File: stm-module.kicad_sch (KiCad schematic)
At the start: 15 parts, among them SW1 Reset, U1 STM32G474RETx, U2 TPS7A20xxxDBV, Y1 Crystal_GND24

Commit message: add crystal
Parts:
- removed Y1: Crystal_GND24, Crystal:Crystal_SMD_5032-4Pin_5.0x3.2mm, symbol Device:Crystal_GND24
- added C10, C11: 15pF, Capacitor_THT:C_Disc_D5.0mm_W2.5mm_P5.00mm, symbol Device:C
- added Y1: Crystal, Crystal:Crystal_SMD_0603-2Pin_6.0x3.5mm, symbol Device:Crystal
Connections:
- net GND: now also C10.1, C11.1
- net at U1.5 (PF0): now also C10.2, Y1.2
- net at U1.6 (PF1): now also C11.2, Y1.1

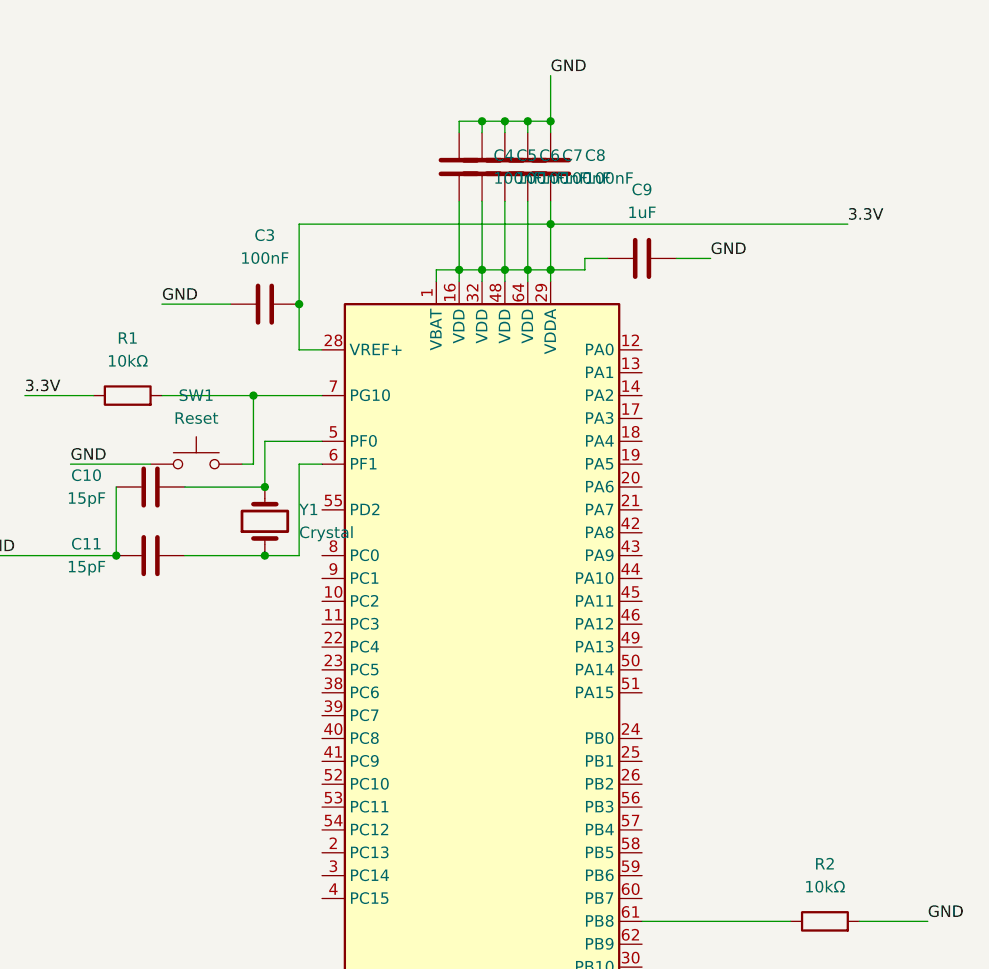
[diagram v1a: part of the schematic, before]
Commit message: add more caps
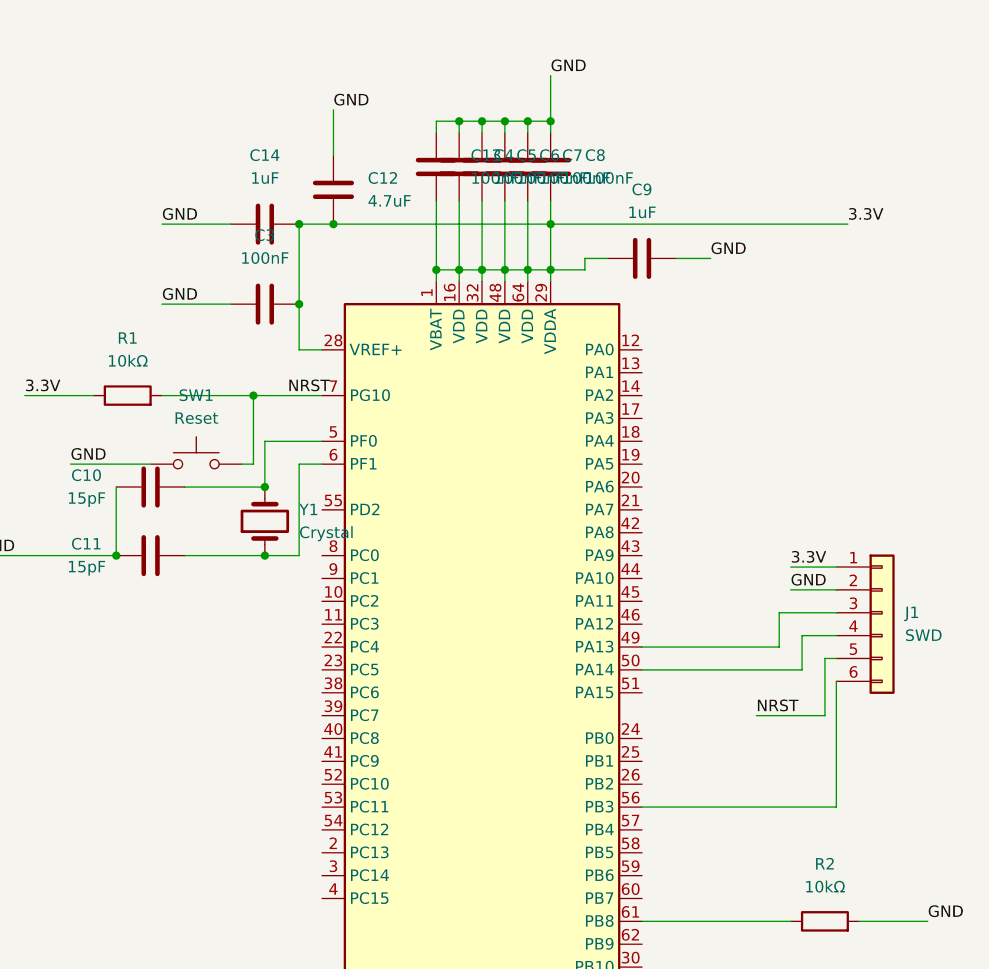
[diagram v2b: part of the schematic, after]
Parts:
- added C12: 4.7uF, Capacitor_SMD:C_0805_2012Metric, symbol Device:C
- added C13: 100nF, Capacitor_SMD:C_0805_2012Metric, symbol Device:C
- added C14: 1uF, Capacitor_SMD:C_0805_2012Metric, symbol Device:C
- added J1: SWD, Connector_PinHeader_2.54mm:PinHeader_1x06_P2.54mm_Vertical, symbol Connector_Generic:Conn_01x06
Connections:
- net 3.3V: now also C12.1, C13.1, C14.2, J1.1 (Pin_1)
- net GND: now also C12.2, C13.2, C14.1, J1.2 (Pin_2)
- net at U1.49 (PA13): now also J1.3 (Pin_3)
- net at U1.50 (PA14): now also J1.4 (Pin_4)
- net at U1.56 (PB3): now also J1.6 (Pin_6)
- net NRST: now reaches R1.2, SW1.2, U1.7 (PG10)
- net NRST: now also J1.5 (Pin_5)

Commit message: pcb work
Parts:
- added J2: connectorL, Connector_PinHeader_2.54mm:PinHeader_2x20_P2.54mm_Vertical, symbol Connector_Generic:Conn_02x20_Odd_Even
- added J3: connectorR, Connector_PinHeader_2.54mm:PinHeader_2x20_P2.54mm_Vertical, symbol Connector_Generic:Conn_02x20_Odd_Even
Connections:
- net GND: now also J2.1 (Pin_1)
- net PC2: now reaches U1.10 (PC2)
- net PC3: now reaches U1.11 (PC3)
- net PA0: now reaches U1.12 (PA0)
- net PA1: now reaches U1.13 (PA1)
- net PA2: now reaches U1.14 (PA2)
- net PA3: now reaches U1.17 (PA3)
- net PA4: now reaches U1.18 (PA4)
- net PA5: now reaches U1.19 (PA5)
- net PC13: now reaches U1.2 (PC13)
- net PA6: now reaches U1.20 (PA6)
- net PA7: now reaches U1.21 (PA7)
- net PC4: now reaches U1.22 (PC4)
- net PC5: now reaches U1.23 (PC5)
- net PB0: now reaches U1.24 (PB0)
- net PB1: now reaches U1.25 (PB1)
- net PB2: now reaches U1.26 (PB2)
- net PC14: now reaches U1.3 (PC14)
- net PB10: now reaches U1.30 (PB10)
- net PB11: now reaches U1.33 (PB11)
- net PB12: now reaches U1.34 (PB12)
- net PB13: now reaches U1.35 (PB13)
- net PB14: now reaches U1.36 (PB14)
- net PB15: now reaches U1.37 (PB15)
- net PC6: now reaches U1.38 (PC6)
- net PC7: now reaches U1.39 (PC7)
- net PC15: now reaches U1.4 (PC15)
- net PC8: now reaches U1.40 (PC8)
- net PC9: now reaches U1.41 (PC9)
- net PA8: now reaches U1.42 (PA8)
- net PA9: now reaches U1.43 (PA9)
- net PA10: now reaches U1.44 (PA10)
- net PA11: now reaches U1.45 (PA11)
- net PA12: now reaches U1.46 (PA12)
- net PA13: now reaches J1.3 (Pin_3), U1.49 (PA13)
- net PA14: now reaches J1.4 (Pin_4), U1.50 (PA14)
- net PA15: now reaches U1.51 (PA15)
- net PC10: now reaches U1.52 (PC10)
- net PC11: now reaches U1.53 (PC11)
- net PC12: now reaches U1.54 (PC12)
- net PD2: now reaches U1.55 (PD2)
- net PB3: now reaches J1.6 (Pin_6), U1.56 (PB3)
- net PB4: now reaches U1.57 (PB4)
- net PB5: now reaches U1.58 (PB5)
- net PB6: now reaches U1.59 (PB6)
- net PB7: now reaches U1.60 (PB7)
- net PB8: now reaches R2.1, U1.61 (PB8)
- net PB9: now reaches U1.62 (PB9)
- net PC0: now reaches U1.8 (PC0)
- net PC1: now reaches U1.9 (PC1)
- net 3.3V renamed +3.3V
- net 5V renamed +5V
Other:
- moved on the sheet: C1, C2, C9, J1, SW1, U2, Y1

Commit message: updates
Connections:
- net +3.3V: now also J3.15 (Pin_15), J3.30 (Pin_30)
- net GND: now also J3.1 (Pin_1), J3.17 (Pin_17), J3.18 (Pin_18), J3.19 (Pin_19), J3.20 (Pin_20), J3.21 (Pin_21), J3.22 (Pin_22), J3.23 (Pin_23), J3.24 (Pin_24), J3.25 (Pin_25), J3.26 (Pin_26), J3.27 (Pin_27), J3.28 (Pin_28)
- net PA10: now also J3.3 (Pin_3)
- net PA11: now also J3.4 (Pin_4)
- net PA12: now also J3.2 (Pin_2)
- net PA3: now also J3.40 (Pin_40)
- net PA4: now also J3.39 (Pin_39)
- net PA5: now also J3.38 (Pin_38)
- net PA6: now also J3.37 (Pin_37)
- net PA7: now also J3.36 (Pin_36)
- net PA8: now also J3.5 (Pin_5)
- net PA9: now also J3.6 (Pin_6)
- net PB0: now also J3.33 (Pin_33)
- net PB1: now also J3.32 (Pin_32)
- net PB10: now also J3.29 (Pin_29)
- net PB11: now also J3.16 (Pin_16)
- net PB12: now also J3.13 (Pin_13)
- net PB13: now also J3.14 (Pin_14)
- net PB14: now also J3.11 (Pin_11)
- net PB15: now also J3.12 (Pin_12)
- net PB2: now also J3.31 (Pin_31)
- net PC4: now also J3.35 (Pin_35)
- net PC5: now also J3.34 (Pin_34)
- net PC6: now also J3.9 (Pin_9)
- net PC7: now also J3.10 (Pin_10)
- net PC8: now also J3.7 (Pin_7)
- net PC9: now also J3.8 (Pin_8)

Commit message: pcb updates
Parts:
- added C15: 10uF, Capacitor_SMD:C_0805_2012Metric, symbol Device:C
- added J4: power, Connector_PinHeader_2.54mm:PinHeader_1x04_P2.54mm_Vertical, symbol Connector:Conn_01x04_Socket
- C12: value 4.7uF -> 10uF
- C13, C3, C4, C5, C6, C7, C8: footprint Capacitor_SMD:C_0805_2012Metric -> Capacitor_SMD:C_0603_1608Metric
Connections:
- net +3.3V: now also C13.2, C4.2, C5.2, C6.2, C7.2, C8.2, J2.16 (Pin_16), J3.17 (Pin_17); no longer C13.1, C4.1, C5.1, C6.1, C7.1, C8.1, J3.15 (Pin_15)
- net +5V: now also C15.1, J4.1 (Pin_1), J4.3 (Pin_3); no longer C2.2
- net GND: now also C13.1, C2.2, C4.1, C5.1, C6.1, C7.1, C8.1, J2.21 (Pin_21), J2.22 (Pin_22), J2.23 (Pin_23), J2.24 (Pin_24), J2.25 (Pin_25), J2.26 (Pin_26), J2.27 (Pin_27), J2.28 (Pin_28), J2.29 (Pin_29), J2.30 (Pin_30), J2.31 (Pin_31), J2.32 (Pin_32), J2.34 (Pin_34), J3.29 (Pin_29), C15.2, J4.2 (Pin_2), J4.4 (Pin_4); no longer C13.2, C4.2, C5.2, C6.2, C7.2, C8.2, J3.17 (Pin_17)
- net PA0: now also J2.37 (Pin_37)
- net PA1: now also J2.40 (Pin_40)
- net PA13: now also J2.2 (Pin_2)
- net PA14: now also J2.3 (Pin_3)
- net PA15: now also J2.4 (Pin_4)
- net PA2: now also J2.39 (Pin_39)
- net PB10: now also J3.15 (Pin_15); no longer J3.29 (Pin_29)
- net PB3: now also J2.9 (Pin_9)
- net PB4: now also J2.10 (Pin_10)
- net PB5: now also J2.11 (Pin_11)
- net PB6: now also J2.12 (Pin_12)
- net PB7: now also J2.13 (Pin_13)
- net PB8: now also J2.14 (Pin_14)
- net PB9: now also J2.15 (Pin_15)
- net PC0: now also J2.33 (Pin_33)
- net PC1: now also J2.36 (Pin_36)
- net PC10: now also J2.5 (Pin_5)
- net PC11: now also J2.6 (Pin_6)
- net PC12: now also J2.7 (Pin_7)
- net PC13: now also J2.17 (Pin_17)
- net PC14: now also J2.18 (Pin_18)
- net PC15: now also J2.19 (Pin_19)
- net PC2: now also J2.35 (Pin_35)
- net PC3: now also J2.38 (Pin_38)
- net PD2: now also J2.8 (Pin_8)
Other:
- moved on the sheet: C12, C2

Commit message: finish main routing
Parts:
- removed J1: SWD, Connector_PinHeader_2.54mm:PinHeader_1x06_P2.54mm_Vertical, symbol Connector_Generic:Conn_01x06
- added J1: Conn_01x05_Pin, Connector_PinHeader_2.54mm:PinHeader_1x05_P2.54mm_Vertical, symbol Connector:Conn_01x05_Pin
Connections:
- net +3.3V: now also J1.5 (Pin_5); no longer J3.30 (Pin_30)
- net GND: now also J3.30 (Pin_30), J1.4 (Pin_4)
- net NRST: now also J1.1 (Pin_1)
- net PA13: now also J1.2 (Pin_2)
- net PA14: now also J1.3 (Pin_3)

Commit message: more pcb updates
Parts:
- added D1: PWR LED, LED_SMD:LED_0805_2012Metric, symbol Device:LED
- added D2: RUN LED, LED_SMD:LED_0805_2012Metric, symbol Device:LED
- added D3: CAN LED, LED_SMD:LED_0805_2012Metric, symbol Device:LED
- added D4: FAULT LED, LED_SMD:LED_0805_2012Metric, symbol Device:LED
- added J5: USB_C_Receptacle_USB2.0_16P, Connector_USB:USB_C_Receptacle_HRO_TYPE-C-31-M-12, symbol Connector:USB_C_Receptacle_USB2.0_16P
- added R3: 330Ω, Resistor_SMD:R_0805_2012Metric, symbol Device:R
- added R4: 220Ω, Resistor_SMD:R_0805_2012Metric, symbol Device:R
- added R5, R6: 1kΩ, Resistor_SMD:R_0805_2012Metric, symbol Device:R
- added R7, R8: 5.1kΩ, Resistor_SMD:R_0805_2012Metric, symbol Device:R
- C1: LCSC Part # (none) -> C107367
- C12: LCSC Part # (none) -> C17024
- C3: LCSC Part # (none) -> C1856507
- R1: LCSC Part # (none) -> C17414
- U1: LCSC Part # (none) -> C521608
- U2: LCSC Part # (none) -> C2862740
- Y1: LCSC Part # (none) -> C18186341
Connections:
- net +3.3V: now also R3.1
- net GND: now also J2.20 (Pin_20), D1.1 (K), D2.1 (K), D3.1 (K), D4.1 (K), J5.A1 (GND), J5.A12 (GND), J5.B1 (GND), J5.B12 (GND), J5.SH (SHIELD), R7.1, R8.1
- net PA3: now also R4.1
- net PA4: now also R5.1
- net PA5: now also R6.1
- net PA11: no longer names the net of J3.4 (Pin_4)
- net PA11: no longer U1.45 (PA11)
- net PA12: no longer names the net of J3.2 (Pin_2)
- net PA12: no longer U1.46 (PA12)
- new net: D1.2 (A), R3.2
- new net: J5.A4 (VBUS), J5.A9 (VBUS), J5.B4 (VBUS), J5.B9 (VBUS)
- new net: J5.A8 (SBU1), R8.2
- new net: J5.B8 (SBU2), R7.2
- new net: D3.2 (A), R5.2
- new net: D4.2 (A), R6.2
- new net: D2.2 (A), R4.2
- new net D+: J5.A6 (D+), J5.B6 (D+), U1.46 (PA12)
- new net D-: J5.A7 (D-), J5.B7 (D-), U1.45 (PA11)

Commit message: final changes
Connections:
- net +3.3V: no longer J3.17 (Pin_17)
- net D+: now also J3.2 (Pin_2)
- net D-: now also J3.4 (Pin_4)
- net GND: now also J3.17 (Pin_17)
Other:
- moved on the sheet: J5, R7, R8
